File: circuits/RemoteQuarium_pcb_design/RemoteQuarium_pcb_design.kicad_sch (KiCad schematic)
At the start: 22 parts, among them J1 Power_terminal, J10 LCD_pins, J11 Feeder_servo_pins, J12 ESP_pins, J13 PH_sensor_sockets, J14 Ph_sesnor-pins, J15 Vcc-GND, J2 ESP left side sockets, J3 ESP right side sockets, J4 Relay_terminal, J5 Calibration_btn, J6 Temp_sensor_socket, J7 Water_sensor_terminal, J8 Light_sensor_terminal, J9 MUX_pins, U1 CD4052BE

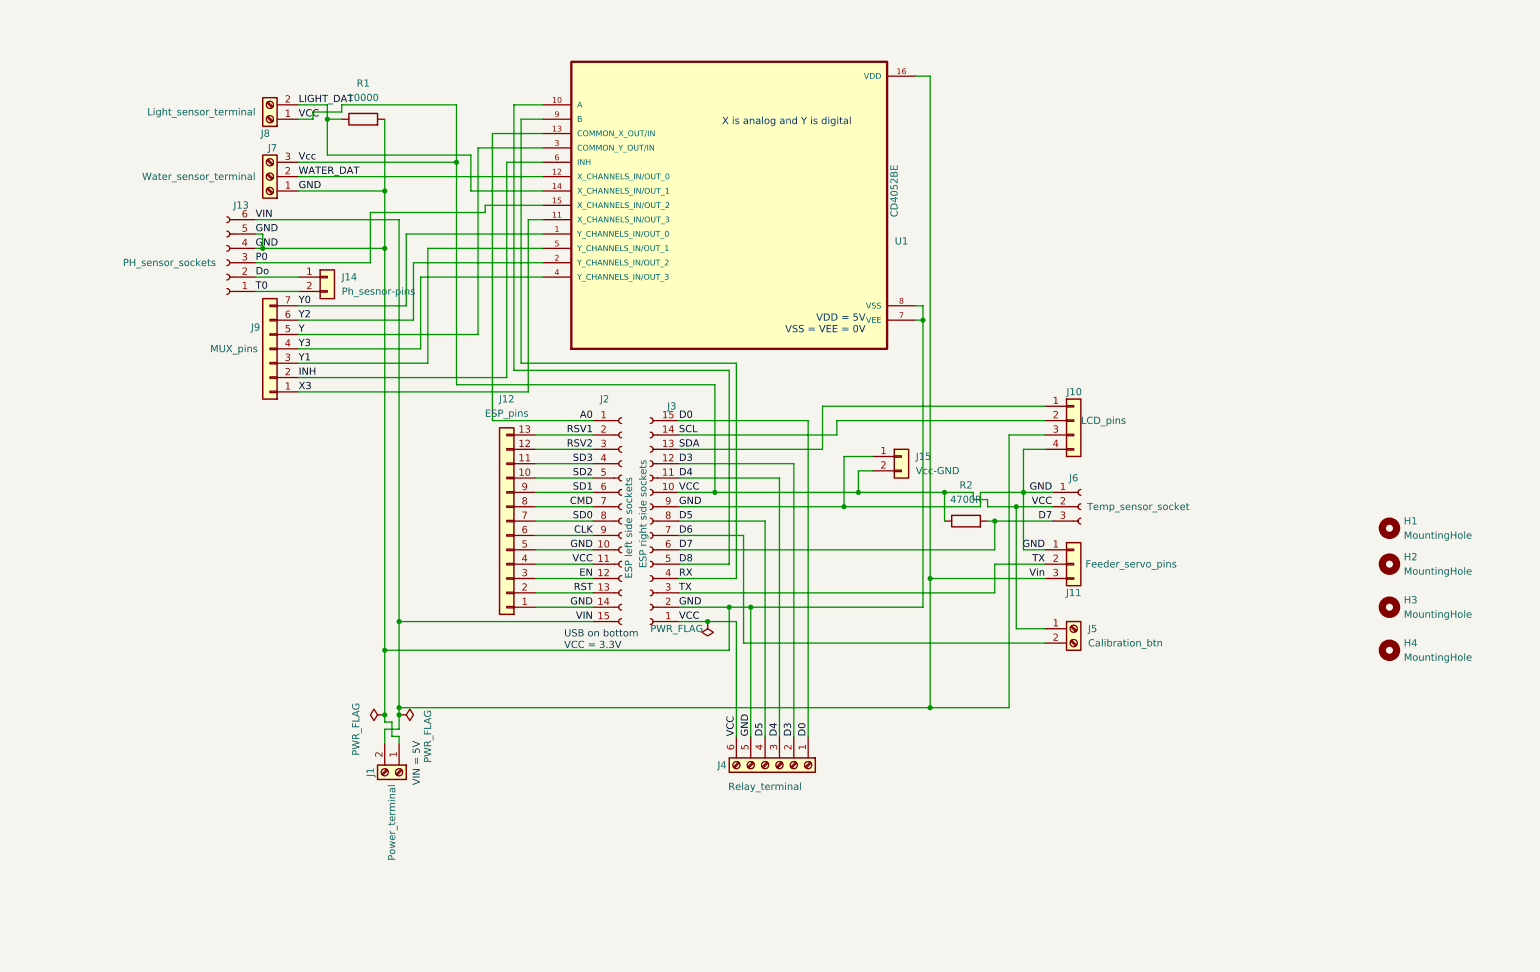
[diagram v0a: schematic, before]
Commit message: Tested the ESP and added logging. Sensor sample selection is not working, need a solution!
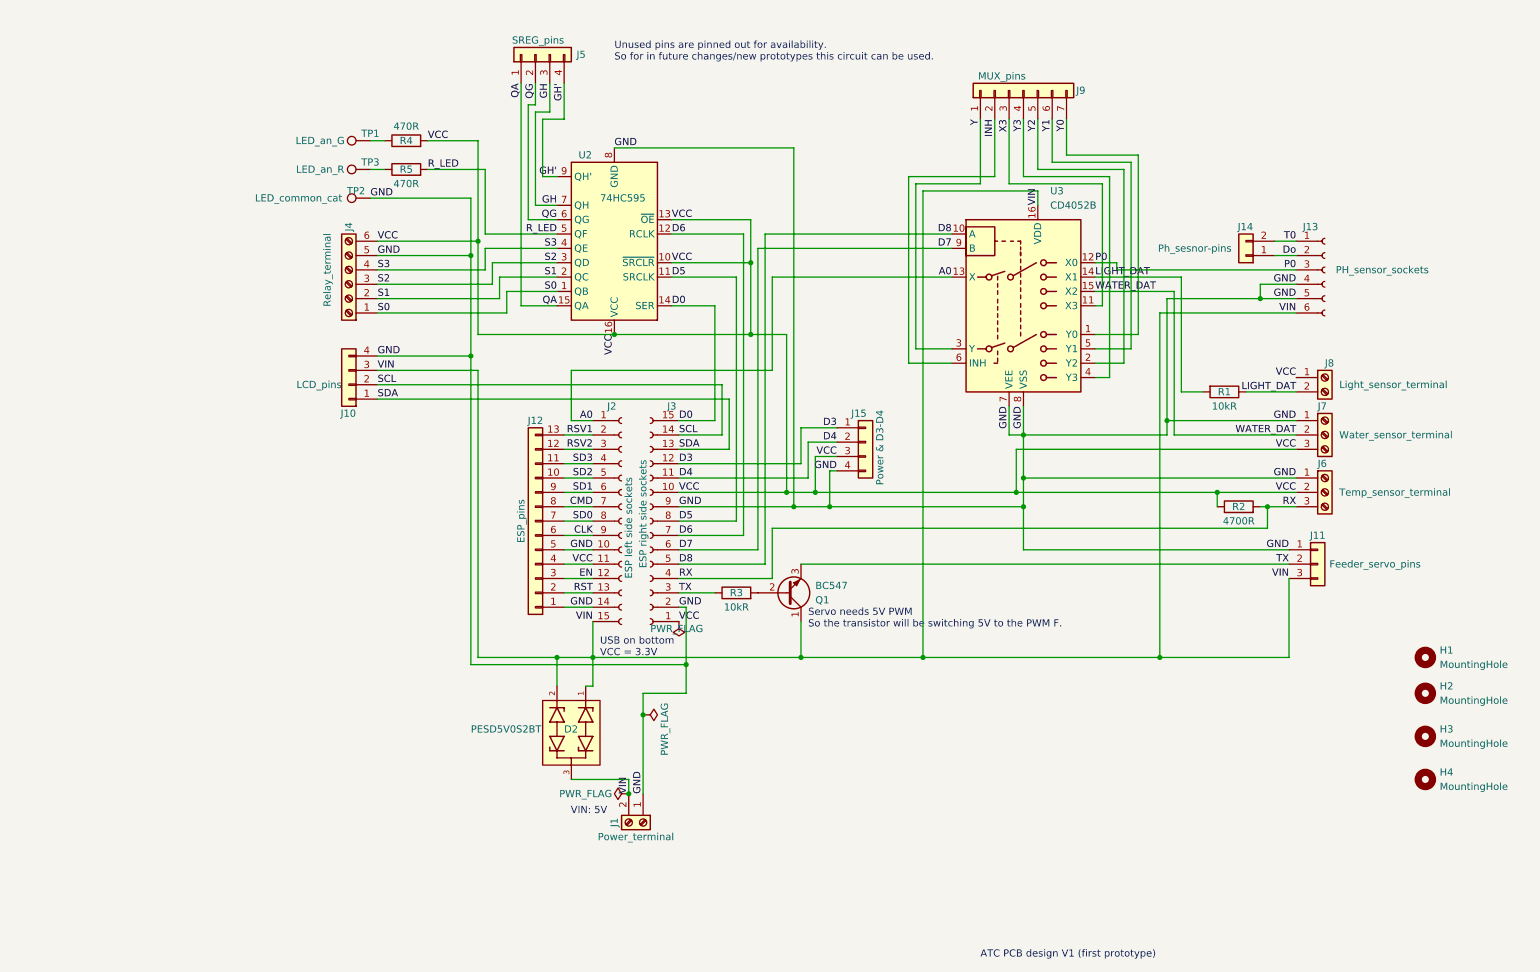
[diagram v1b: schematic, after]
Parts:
- removed J15: Vcc-GND, Connector_PinHeader_2.54mm:PinHeader_1x02_P2.54mm_Vertical, symbol Connector_Generic:Conn_01x02
- removed J5: Calibration_btn, TerminalBlock_Phoenix:TerminalBlock_Phoenix_MPT-0,5-2-2.54_1x02_P2.54mm_Horizontal, symbol Connector:Screw_Terminal_01x02
- removed J6: Temp_sensor_socket, Connector_PinSocket_2.54mm:PinSocket_1x03_P2.54mm_Horizontal, symbol Connector:Conn_01x03_Socket
- removed U1: CD4052BE, Socket:DIP_Socket-16_W4.3_W5.08_W7.62_W10.16_W10.9_3M_216-3340-00-0602J, symbol CD4052BE:CD4052BE
- added D2: PESD5V0S2BT, PESD5V0S2BT:SOT23, symbol PESD5V0S2BT:PESD5V0S2BT
- added J15: Power & D3-D4, Connector_PinHeader_2.54mm:PinHeader_1x04_P2.54mm_Vertical, symbol Connector_Generic:Conn_01x04
- added J5: SREG_pins, Connector_PinHeader_2.54mm:PinHeader_1x04_P2.54mm_Vertical, symbol Connector_Generic:Conn_01x04
- added J6: Temp_sensor_terminal, TerminalBlock_Phoenix:TerminalBlock_Phoenix_MPT-0,5-3-2.54_1x03_P2.54mm_Horizontal, symbol Connector:Screw_Terminal_01x03
- added Q1: BC547, Package_TO_SOT_THT:TO-92_Inline, symbol Transistor_BJT:BC547
- added R3: 10kR, Resistor_THT:R_Axial_DIN0207_L6.3mm_D2.5mm_P5.08mm_Vertical, symbol Device:R
- added R4, R5: 470R, Resistor_THT:R_Axial_DIN0207_L6.3mm_D2.5mm_P5.08mm_Vertical, symbol Device:R
- added TP1: LED_an_G, TestPoint:TestPoint_2Pads_Pitch2.54mm_Drill0.8mm, symbol Connector:TestPoint
- added TP2: LED_common_cat, TestPoint:TestPoint_2Pads_Pitch2.54mm_Drill0.8mm, symbol Connector:TestPoint
- added TP3: LED_an_R, TestPoint:TestPoint_2Pads_Pitch2.54mm_Drill0.8mm, symbol Connector:TestPoint
- added U2: 74HC595, CD4052BE:DIP794W45P254L1969H508Q16, symbol 74xx:74HC595
- added U3: CD4052B, CD4052BE:DIP794W45P254L1969H508Q16, symbol Analog_Switch:CD4052B
- R1: value 10000 -> 10kR
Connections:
- net A0: now also U3.13 (X)
- net D0: now also U2.14 (SER); no longer J4.1 (Pin_1)
- net D3: now also J15.1 (Pin_1); no longer J4.2 (Pin_2)
- net D4: now also J15.2 (Pin_2); no longer J4.3 (Pin_3)
- net D5: now also U2.11 (SRCLK); no longer J4.4 (Pin_4)
- net D6: now also U2.12 (RCLK)
- net D7: now also U3.9 (B); no longer R2.2
- net D8: now also U3.10 (A)
- net GND: now also J15.4 (Pin_4), J6.1 (Pin_1), TP2.1, U2.8 (GND), U3.7 (VEE), U3.8 (VSS); no longer R1.2
- net INH: now also U3.6 (INH)
- net LIGHT_DAT: now also R1.2, U3.14 (X1)
- net P0: now also U3.12 (X0)
- net RX: now also R2.2, J6.3 (Pin_3)
- net TX: now also Q1.3 (E), R3.1
- net VCC: now also J15.3 (Pin_3), J6.2 (Pin_2), R4.2, U2.10 (~{SRCLR}), U2.13 (~{OE}), U2.16 (VCC)
- net VIN: now also D2.1, D2.2, D2.3, Q1.1 (C), U3.16 (VDD)
- net WATER_DAT: now also U3.15 (X2)
- net X3: now also J9.3 (Pin_3), U3.11 (X3); no longer J9.1 (Pin_1)
- net Y: now also J9.1 (Pin_1), U3.3 (Y); no longer J9.5 (Pin_5)
- net Y0: now also U3.1 (Y0)
- net Y1: now also J9.6 (Pin_6), U3.5 (Y1); no longer J9.3 (Pin_3)
- net Y2: now also J9.5 (Pin_5), U3.2 (Y2); no longer J9.6 (Pin_6)
- net Y3: now also U3.4 (Y3)
- new net: Q1.2 (B), R3.2
- new net: R4.1, TP1.1
- new net: R5.1, TP3.1
- new net GH: J5.3 (Pin_3), U2.7 (QH)
- new net GH': J5.4 (Pin_4), U2.9 (QH')
- new net QA: J5.1 (Pin_1), U2.15 (QA)
- new net QG: J5.2 (Pin_2), U2.6 (QG)
- new net R_LED: R5.2, U2.5 (QF)
- new net S0: J4.1 (Pin_1), U2.1 (QB)
- new net S1: J4.2 (Pin_2), U2.2 (QC)
- new net S2: J4.3 (Pin_3), U2.3 (QD)
- new net S3: J4.4 (Pin_4), U2.4 (QE)
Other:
- note added: "ATC PCB design V1 (first prototype)"
- note added: "Servo needs 5V PWM So the transistor will be switching 5V to the PWM F."
- note added: "Unused pins are pinned out for availability. So for in future changes/new prototypes this circuit can be used."
- note added: "VIN: 5V"
- note removed: "VDD = 5V VSS = VEE = 0V"
- note removed: "VIN = 5V"
- note removed: "X is analog and Y is digital"
- moved on the sheet: H1, H2, H3, H4, J1, J10, J11, J12, J13, J14, J4, J7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

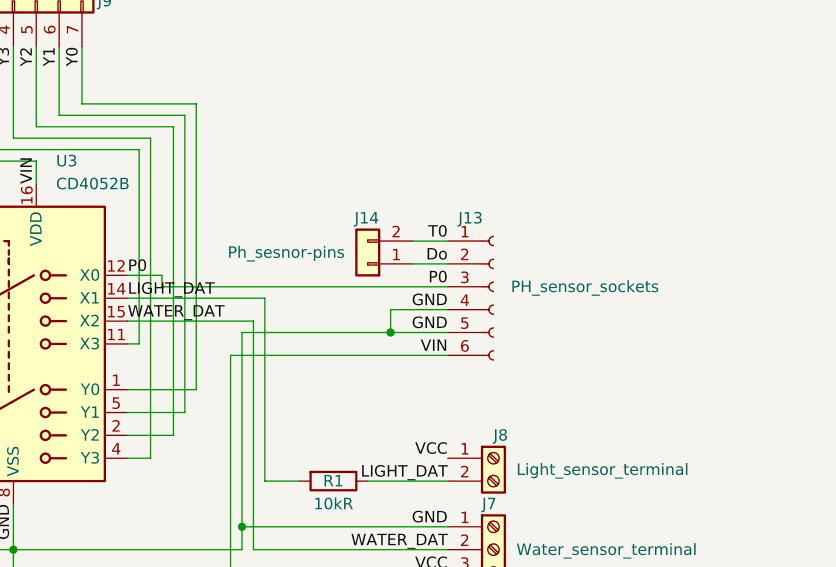
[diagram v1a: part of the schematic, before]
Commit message: Solved hour sample time problem, also stats weekly label porblem, changed some colors and added profile updater service, but no handle of the actions.
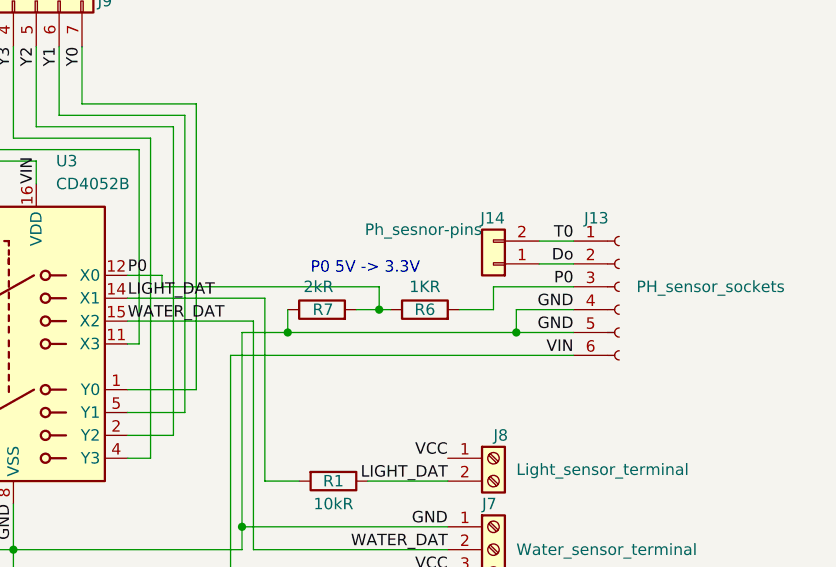
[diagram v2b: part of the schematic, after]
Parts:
- added R6: 1KR, symbol Device:R
- added R7: 2kR, symbol Device:R
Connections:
- net GND: now also R7.1
- net P0: now also R6.1, R6.2, R7.2
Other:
- note added: "P0 5V -> 3.3V"
- moved on the sheet: J13, J14

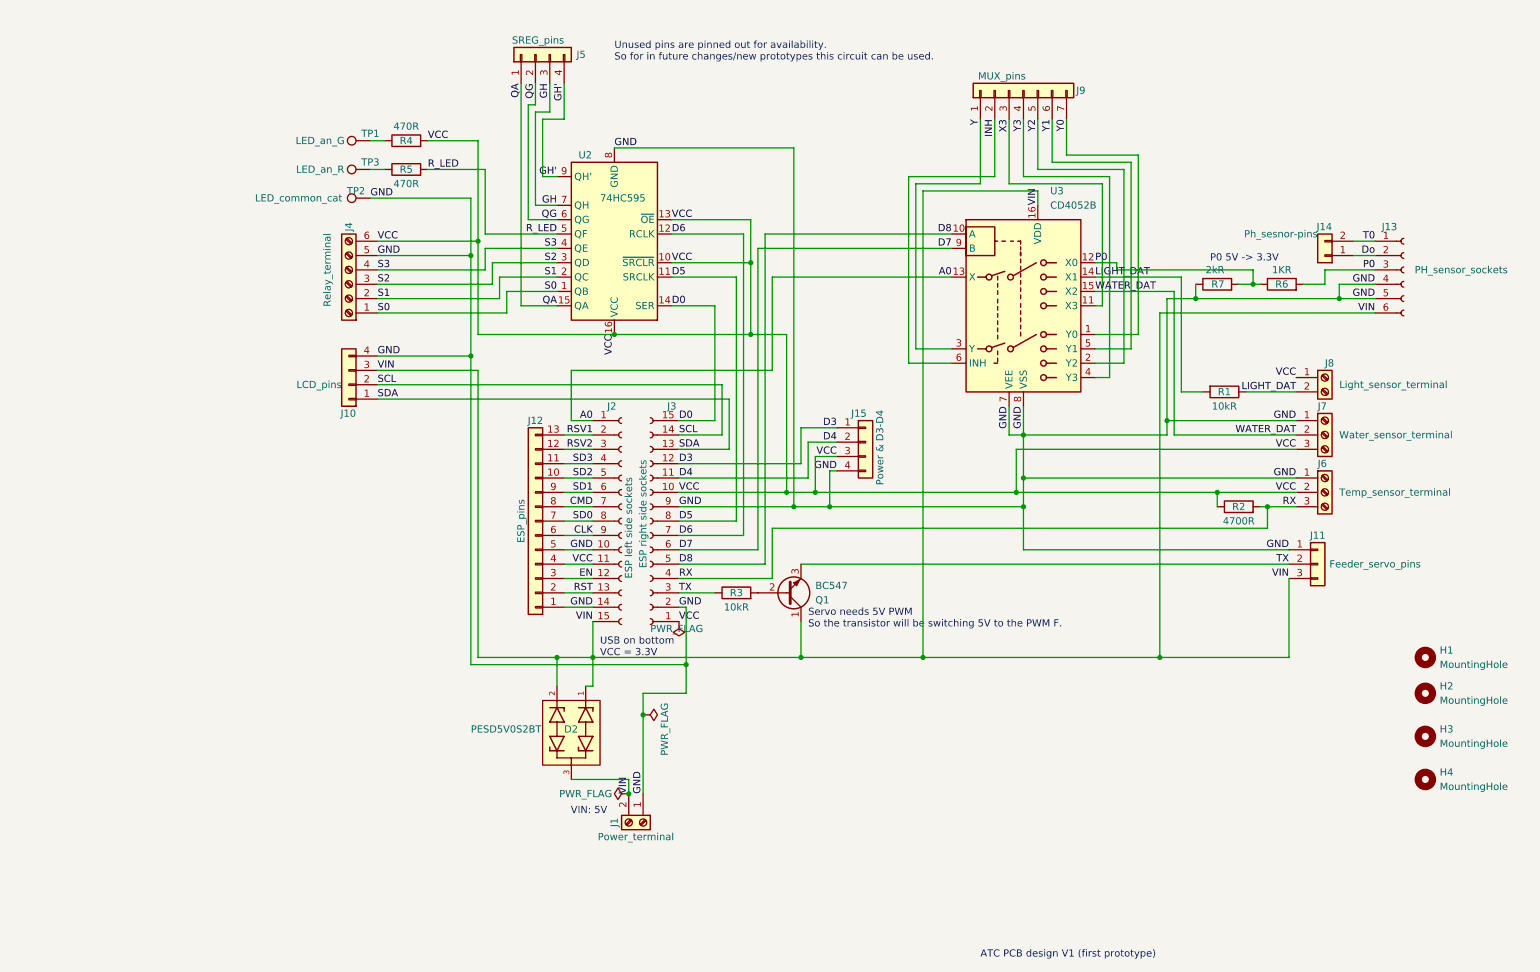
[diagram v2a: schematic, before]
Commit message: Fixed ESP memory leak xd. Fixed wrong samplePeriod enum numbering. Fixed up relay switching. Also added WDT and runtime measuring. Fixed up wrong time formatting in app. Fixed a lot of stuff actually xdd
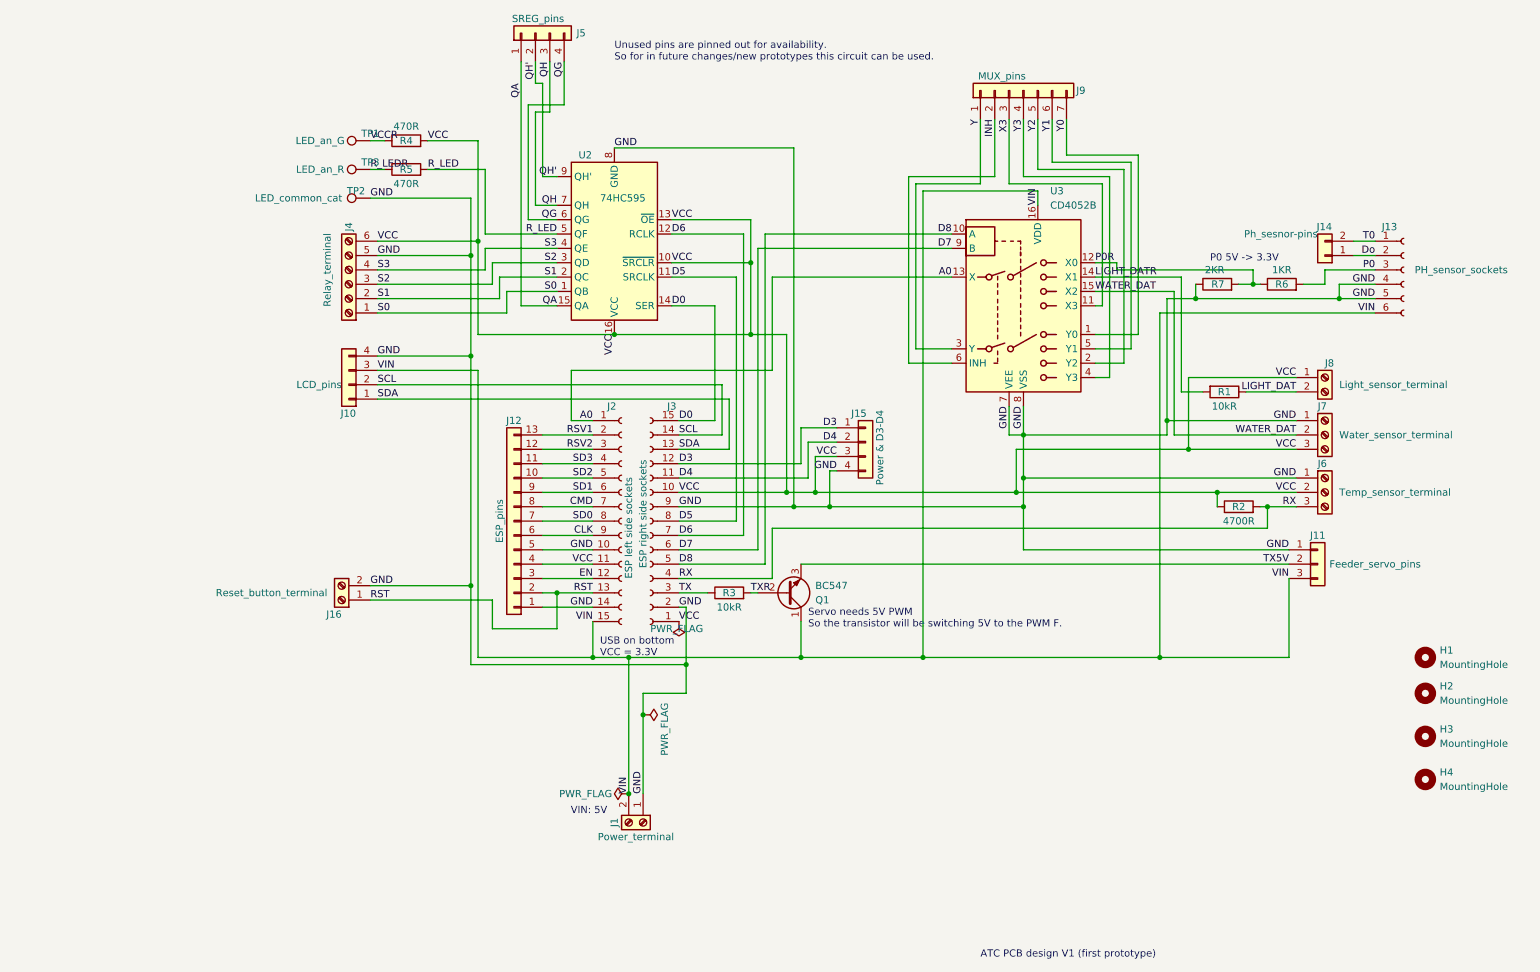
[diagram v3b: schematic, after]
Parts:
- removed D2: PESD5V0S2BT, PESD5V0S2BT:SOT23, symbol PESD5V0S2BT:PESD5V0S2BT
- added J16: Reset_button_terminal, TerminalBlock_Phoenix:TerminalBlock_Phoenix_MPT-0,5-2-2.54_1x02_P2.54mm_Horizontal, symbol Connector:Screw_Terminal_01x02
- R3, R4, R5: footprint Resistor_THT:R_Axial_DIN0207_L6.3mm_D2.5mm_P5.08mm_Vertical -> Resistor_THT:R_Axial_DIN0204_L3.6mm_D1.6mm_P5.08mm_Horizontal
- R6: footprint (none) -> Resistor_THT:R_Axial_DIN0204_L3.6mm_D1.6mm_P5.08mm_Horizontal
- R7: value 2kR -> 2KR; footprint (none) -> Resistor_THT:R_Axial_DIN0204_L3.6mm_D1.6mm_P5.08mm_Horizontal
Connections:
- net GND: now also J16.2 (Pin_2)
- net LIGHT_DAT: no longer R1.2, U3.14 (X1)
- net P0: no longer R6.1, R7.2, U3.12 (X0)
- net QG: now also J5.4 (Pin_4); no longer J5.2 (Pin_2)
- net RST: now also J16.1 (Pin_1)
- net TX: no longer J11.2 (Pin_2), Q1.3 (E)
- net TXR: now reaches Q1.2 (B), R3.2
- net VCCR: now reaches R4.1, TP1.1
- net R_LEDR: now reaches R5.1, TP3.1
- net GH renamed QH
- net GH' renamed QH'
- net QH': now also J5.2 (Pin_2); no longer J5.4 (Pin_4)
- new net LIGHT_DATR: R1.2, U3.14 (X1)
- new net P0R: R6.1, R7.2, U3.12 (X0)
- new net TX5V: J11.2 (Pin_2), Q1.3 (E)
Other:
- moved on the sheet: J12, J5, R3

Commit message: Added more complex logging and notification testing should work, app builds and is usable, but need to add react SVG libs for the charts to workgit add .
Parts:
- added Q2, Q3, Q4, Q5: BC547, Package_TO_SOT_THT:TO-92_Inline, symbol Transistor_BJT:BC547
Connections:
- net S0: now also Q5.2 (B); no longer J4.1 (Pin_1)
- net S1: now also Q4.2 (B); no longer J4.2 (Pin_2)
- net S2: now also Q3.2 (B); no longer J4.3 (Pin_3)
- net S3: now also Q2.2 (B); no longer J4.4 (Pin_4)
- net VCC: no longer J4.6 (Pin_6)
- net VIN: now also J4.6 (Pin_6), Q2.1 (C), Q3.1 (C), Q4.1 (C), Q5.1 (C)
- new net S05V: J4.1 (Pin_1), Q5.3 (E)
- new net S15V: J4.2 (Pin_2), Q4.3 (E)
- new net S25V: J4.3 (Pin_3), Q3.3 (E)
- new net S35V: J4.4 (Pin_4), Q2.3 (E)
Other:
- moved on the sheet: J10, J4
